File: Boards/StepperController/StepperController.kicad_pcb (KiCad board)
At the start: 2 copper layers, 160 x 100 mm, 189 parts, among them IC1 ATMEGA645A-A, J1 I2C, J2 SPI_Extern, J3 ISP, J4 Reference, J5 Display, J6 Ext, J7 Spindle, P1 Power, P10 CONN_Z, P2 Cover, P3 USB_B, P4 Relay2, P5 Relay1, P6 Emer_Off, P8 CONN_X, P9 CONN_Y, Q1 BC817-40, Q2 BC817-40, Q3 BC817-40, Q4 BC817-40, Q5 BC817-40, Q6 BC807-40, Q7 BC807-40, Q8 BC817-40, SW2 SW_1, SW3 SW_2, U1 LM2576S-5, U2 74HC11, U3 FT232RL, U4 74HC08, U5 TMC2660, U6 TMC2660, U7 TMC2660, X1 16MHz, Y1 20MHz

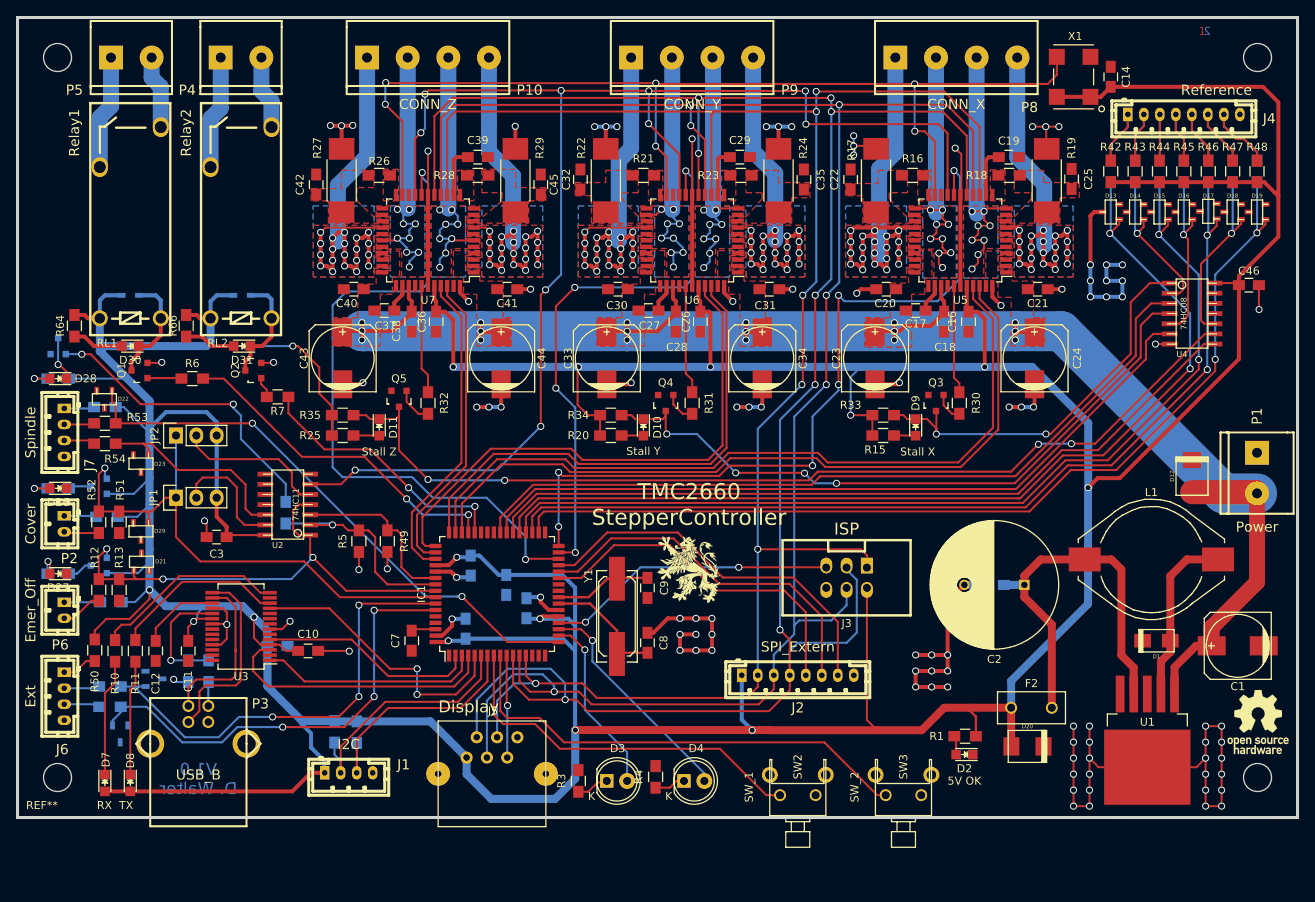
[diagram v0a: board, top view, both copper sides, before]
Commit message: Added Reset Logic, Layout changes
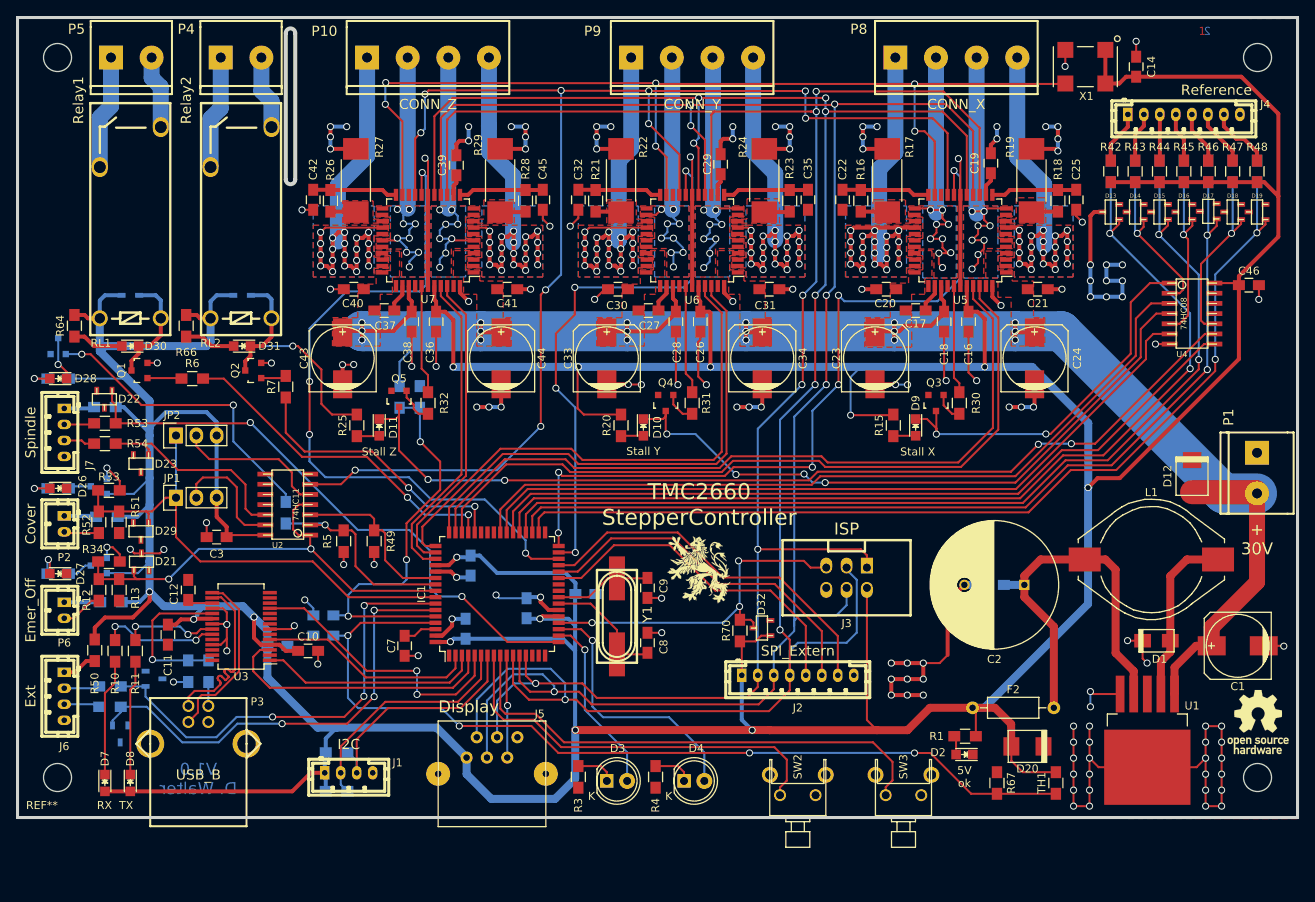
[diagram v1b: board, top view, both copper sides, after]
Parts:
- removed R35: 10k, Resistors_SMD:R_0805_HandSoldering
- added C48: 100nF, Capacitors_SMD:C_0805_HandSoldering, B.Cu at (102.2, 130.2)
- added C49: 100nF, Capacitors_SMD:C_0805_HandSoldering, B.Cu at (102.2, 127.6)
- added D32: ZMY5.6, w_smd_trans:sot23, F.Cu at (157.1, 129.2)
- added R67: 3k6, Resistors_SMD:R_0805_HandSoldering, F.Cu at (186.4, 148.6)
- added R68: 8k6, Resistors_SMD:R_0805_HandSoldering, B.Cu at (111.8, 100.3)
- added R69: 1k2, Resistors_SMD:R_0805_HandSoldering, B.Cu at (114.3, 100.3)
- added R70: 12k, Resistors_SMD:R_0805_HandSoldering, F.Cu at (154.3, 129.5)
- added TH1: 6k8, Resistors_SMD:R_0805_HandSoldering, F.Cu at (193.8, 148.6)
- C22, C25, C35, C42, C45: value 470nF -> 10nF
- C8, C9: value 12pF -> 22pF
- D26, D27: value LED -> LED_Rd
- D28, D30, D31: value LED -> LED_Gn
- F2: footprint Fuse_Holders_and_Fuses:Fuse_TE5_Littlefuse-395Series -> Resistors_ThroughHole:R_Axial_DIN0207_L6.3mm_D2.5mm_P10.16mm_Horizontal
- R1, R3, R62, R64, R66: value 160R -> 140R
- R10, R11: value 270R -> 150R
- R13, R51: value 1k -> 3k6
- R16, R18, R23, R26, R28: value 10R -> 22R
- R17, R19, R24, R27, R29: value 150mR -> 100mR
- R30, R31, R32: value 10k -> 4k7
- R33, R34: value 10k -> 1k
- R42, R43, R44, R45, R46, R47, R48, R65: value 1k -> 4k7
- R49, R5: value 1k -> 10k
- Y1: value 20MHz -> 16MHz; footprint Crystals:Q_49U3HMS -> w_crystal:hc-49_smd
- moved R33 97.2 mm to (75.4, 112.0)
- moved R34 65.3 mm to (75.4, 120.9), turned to 0 degrees
- moved C47 9.97 mm to (135.0, 125.0), turned to 0 degrees
- moved C12 8.64 mm to (85.3, 124.5), turned to 90 degrees
- moved R56 7.42 mm to (103.9, 149.6), turned to 0 degrees
- moved R16 7.21 mm to (169.4, 75.8), turned to 90 degrees
- moved R18 6.87 mm to (194.1, 75.8), turned to 90 degrees
- moved R23 6.87 mm to (160.5, 75.8), turned to 90 degrees
- moved R26 6.87 mm to (103.1, 75.8), turned to 90 degrees
- moved R21 6.76 mm to (136.3, 75.8), turned to 90 degrees
- moved R28 6.76 mm to (127.5, 75.8), turned to 90 degrees
- moved R57 3.59 mm to (103.9, 144.8), turned to 0 degrees
- moved C14 3.42 mm to (203.8, 59.1)
- moved C11 3.25 mm to (82.8, 130.0)
- moved C39 2.85 mm to (118.9, 71.4), turned to 90 degrees
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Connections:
- net /Driver/Driver_X/TMC_Clock renamed /Driver/TMC_Clock
- net /Driver/Driver_X/TMC_Enable renamed /Driver/TMC_Enable
- net Net-(D3-Pad2) renamed /Controller/LED1
- net Net-(D4-Pad2) renamed /Controller/LED2
- net Net-(IC1-Pad20) renamed /Controller/Reset
- net Net-(IC1-Pad27) renamed /Controller/CS_Ext1
- net Net-(IC1-Pad28) renamed /Controller/CS_Ext2
- net Net-(IC1-Pad29) renamed /Controller/CS_Ext3
- net Net-(IC1-Pad38) renamed /Controller/RefZ2
- net Net-(IC1-Pad39) renamed /Controller/RefY2
- net Net-(IC1-Pad40) renamed /Controller/RefX2
- net Net-(IC1-Pad6) renamed /Controller/SCL
- net Net-(IC1-Pad7) renamed /Controller/SDA
- net Net-(IC1-Pad8) renamed /Controller/Button1
- net Net-(IC1-Pad9) renamed /Controller/Button2
- net Net-(P3-Pad1) renamed /Interface/VCC_USB
- net Net-(P3-Pad2) renamed /Interface/D-
- net Net-(P3-Pad3) renamed /Interface/D+
- net Net-(R8-Pad2) renamed /Interface/Reset_UART
- C22 pad 2: /Driver/Driver_X/BRB_X -> /Driver/Driver_X/SRB_X
- C25 pad 2: /Driver/Driver_X/BRA_X -> /Driver/Driver_X/SRA_X
- C32 pad 2: /Driver/Driver_Y/BRB_Y -> /Driver/Driver_Y/SRB_Y
- C35 pad 2: /Driver/Driver_Y/BRA_Y -> /Driver/Driver_Y/SRA_Y
- C42 pad 2: /Driver/Driver_Z/BRB_Z -> /Driver/Driver_Z/SRB_Z
- C45 pad 2: /Driver/Driver_Z/BRA_Z -> /Driver/Driver_Z/SRA_Z
- IC1 pad 60: (no net) -> /Controller/V_SUP
- IC1 pad 61: (no net) -> /Controller/T_REG
- Q6 pad 1: /Controller/Cover -> Net-(Q6-Pad1)
- Q7 pad 1: /Controller/Emergency_Off -> Net-(Q7-Pad1)
- R10 pad 2: Net-(R10-Pad2) -> /Interface/LED_TX
- R11 pad 2: Net-(R11-Pad2) -> /Interface/LED_RX
- R3 pad 1: Net-(D3-Pad1) -> GND
- R3 pad 2: GND -> Net-(D3-Pad1)
- R33 pad 1: +5V -> /Controller/Cover
- R33 pad 2: /Controller/Stall_X -> Net-(Q6-Pad1)
- R34 pad 1: /Controller/Stall_Y -> /Controller/Emergency_Off
- R34 pad 2: +5V -> Net-(Q7-Pad1)
- R4 pad 1: Net-(D4-Pad1) -> GND
- R4 pad 2: GND -> Net-(D4-Pad1)
- SW2 pad 3: GND -> (no net)
- SW3 pad 3: GND -> (no net)
- U3 pad 12: Net-(R11-Pad2) -> (no net)
- U3 pad 14: Net-(R10-Pad2) -> (no net)
- U3 pad 22: (no net) -> /Interface/LED_RX
- U3 pad 23: (no net) -> /Interface/LED_TX
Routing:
- net /Controller/T_REG: track 0.00 -> 114.7 mm, vias 0 -> 4
- net GND: track 307.5 -> 397.8 mm, vias 103 -> 138
- net /Controller/V_SUP: track 0.00 -> 50.4 mm, vias 0 -> 3
- net Net-(R10-Pad2): track 24.2 -> 0.00 mm
- net Net-(R11-Pad2): track 21.8 -> 0.00 mm
- net /Interface/LED_TX: track 0.00 -> 14.9 mm, vias 0 -> 2
- net +5V: track 751.0 -> 765.1 mm
- net /Interface/LED_RX: track 0.00 -> 12.0 mm, vias 0 -> 2
- net /Driver/Driver_X/SRB_X: track 0.00 -> 11.0 mm
- net /Driver/Driver_X/SRA_X: track 0.00 -> 10.7 mm
- net /Driver/Driver_Y/SRA_Y: track 0.00 -> 10.7 mm
- net /Driver/Driver_Z/SRB_Z: track 0.00 -> 10.6 mm
- net /Driver/Driver_Z/SRA_Z: track 0.00 -> 10.6 mm
- net /Driver/Driver_Y/SRB_Y: track 0.00 -> 10.5 mm
- net /Controller/Reset: track 36.5 -> 45.0 mm, vias 2 -> 3
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- removed copper zone on F.Cu, net /Driver/Driver_X/SRA_X
- removed copper zone on F.Cu, net /Driver/Driver_X/SRB_X
- removed copper zone on F.Cu, net /Driver/Driver_Y/SRA_Y
- removed copper zone on F.Cu, net /Driver/Driver_Y/SRB_Y
- removed copper zone on F.Cu, net /Driver/Driver_Z/SRA_Z
- removed copper zone on F.Cu, net /Driver/Driver_Z/SRB_Z
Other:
- board text added: "+ 30V"
- board text added: "5V ok"
- board text removed: "5V OK"

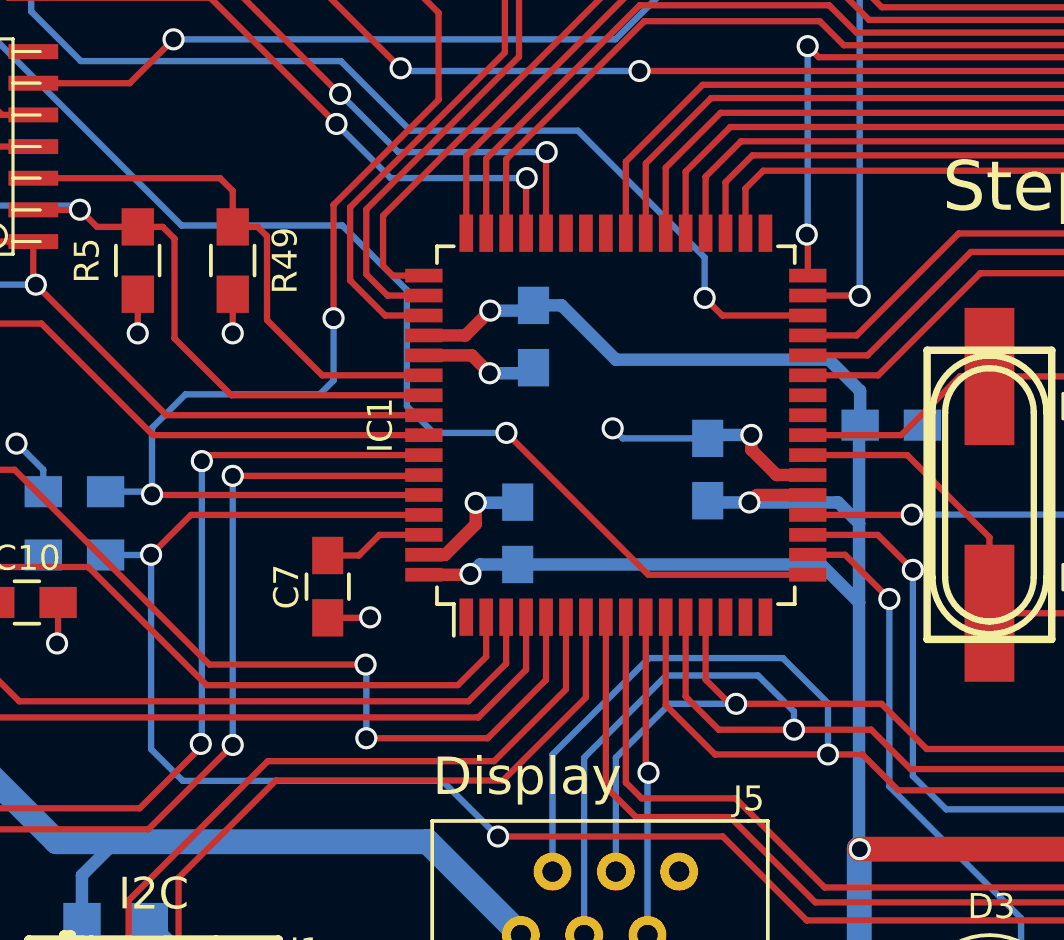
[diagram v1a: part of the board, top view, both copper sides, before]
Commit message: Removed Accidental commit, changed µC to ATMega128A
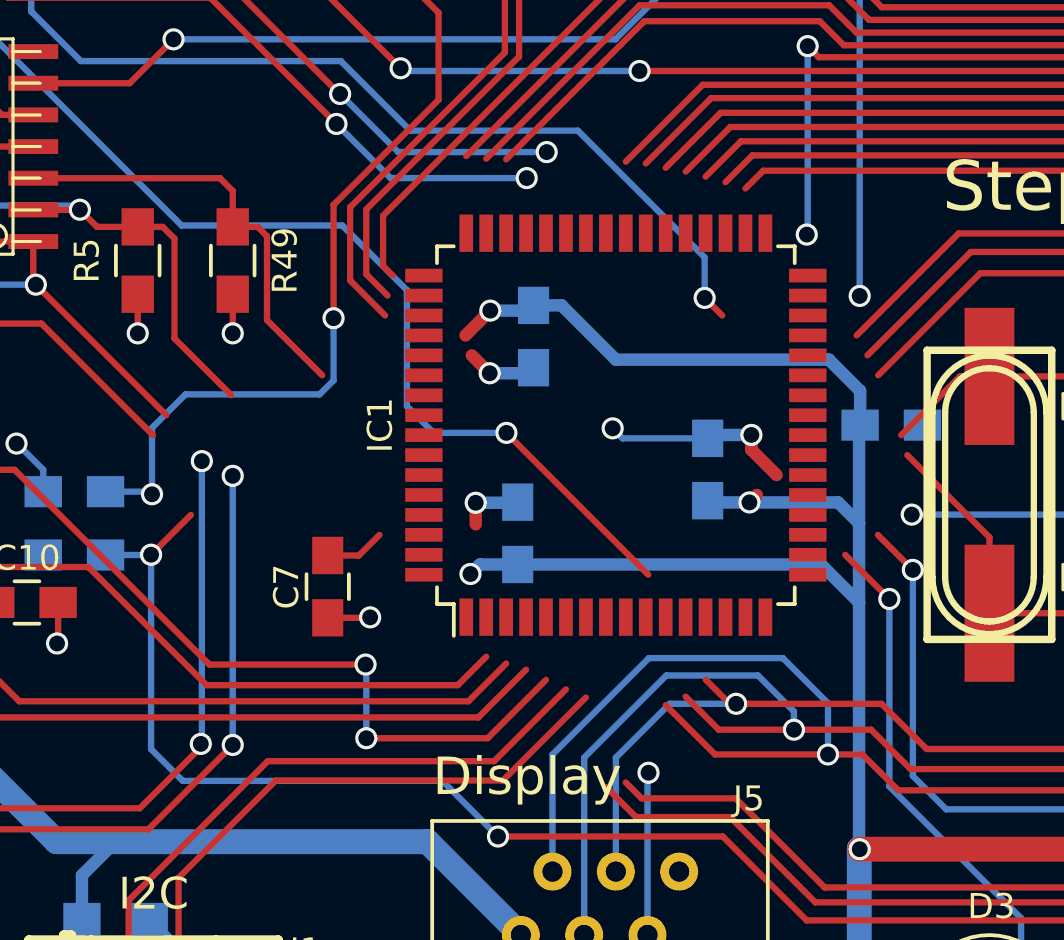
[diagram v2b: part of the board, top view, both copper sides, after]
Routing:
- net /Controller/V_SUP: track 50.4 -> 39.5 mm
- net /Controller/Cover: track 63.1 -> 52.3 mm
- net /Controller/Emergency_Off: track 58.7 -> 48.3 mm
- net /Controller/T_REG: track 114.7 -> 105.3 mm
- net /Controller/Ext1: track 56.4 -> 47.7 mm
- net /Interface/Spindle_Enable: track 26.1 -> 18.4 mm
- net /Controller/Ext2: track 57.1 -> 49.5 mm
- net /Controller/Button1: track 50.8 -> 44.0 mm
- net /Controller/Button2: track 62.9 -> 56.3 mm
- net /Controller/Spindle_PWM: track 73.8 -> 67.4 mm
- net /Interface/CS_Disp: track 12.8 -> 6.68 mm
- net GND: track 397.8 -> 392.0 mm
- net +5V: track 765.1 -> 759.5 mm
- net /Controller/Reset: track 45.0 -> 40.9 mm
- net /Controller/Enable: track 21.8 -> 17.7 mm
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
